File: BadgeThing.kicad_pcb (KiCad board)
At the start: 2 copper layers, 78.7 x 40.2 mm, 67 parts, among them J1 USB_C_Receptacle_USB2.0, J2 Connector_Generic_Conn_01x02, J3 Ext 5V, J4 SWD Header, J6 External 3V3, SW1 BOOTSEL, SW2 ESP RESET, SW3 Left, SW4 Down, SW5 Select, SW6 Up, SW7 Right, U2 W25Q32JVSS, U3 RP2040, U4 NCP1117-3.3_SOT223, U5 ESP-12F, Y1 12.000MHz

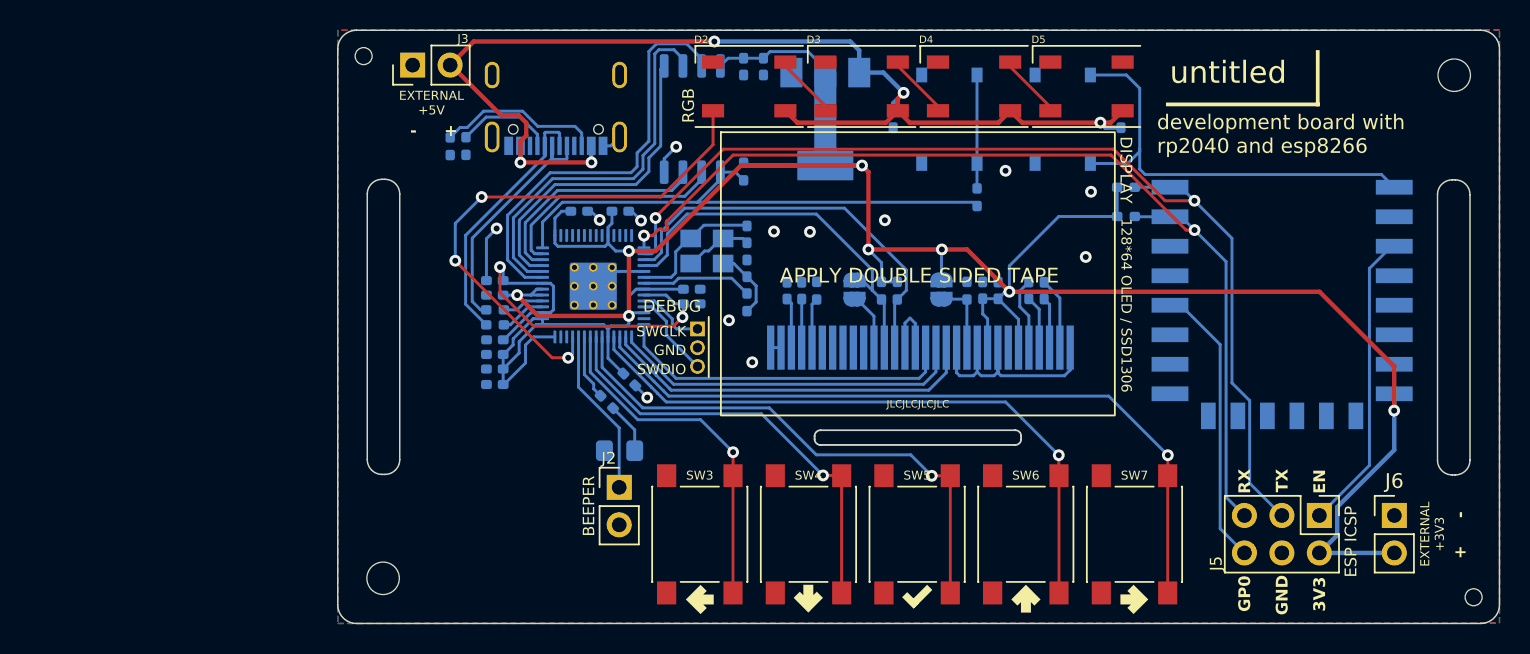
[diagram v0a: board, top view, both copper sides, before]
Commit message: Begin re-routing, updated ssd1306 pinout (not backwards anymore)
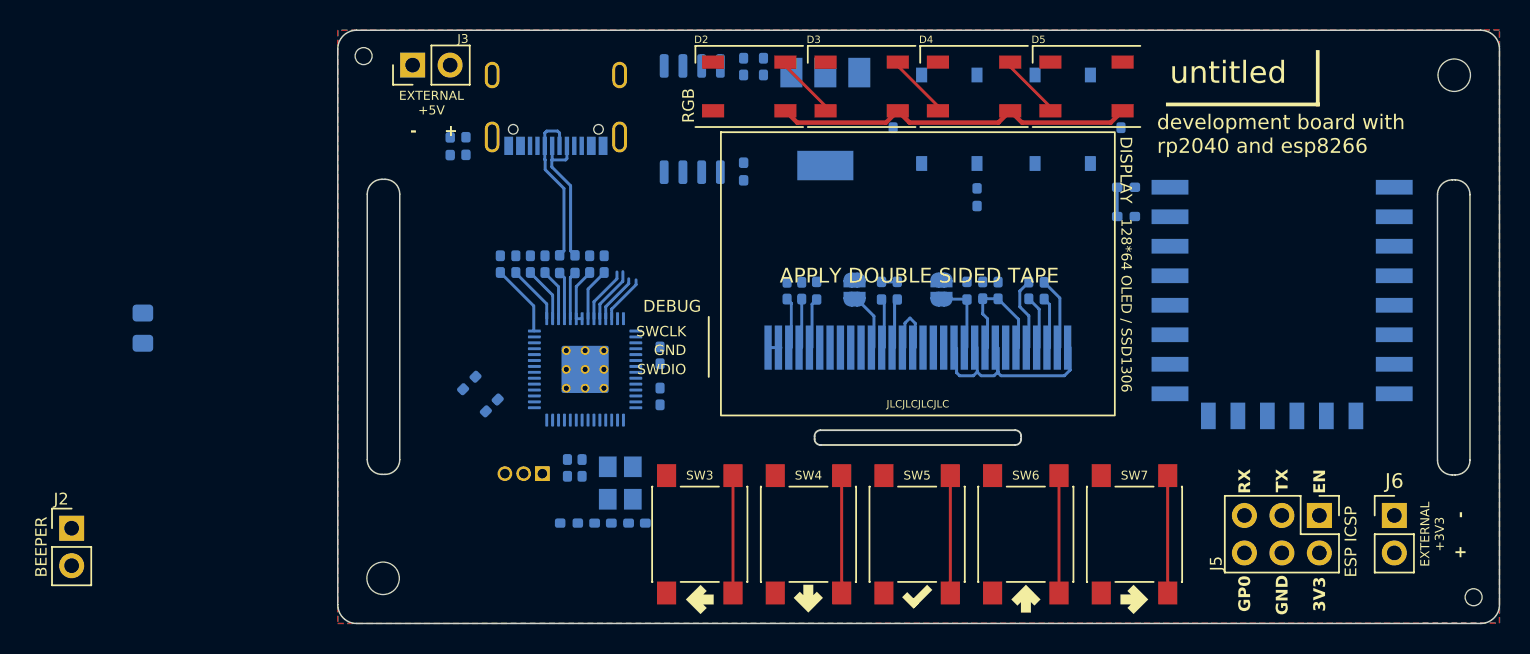
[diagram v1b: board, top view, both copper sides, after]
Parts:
- moved J2 37.2 mm to (104.4, 127.6)
- moved D1 33.4 mm to (109.2, 114.0), turned to -90 degrees
- moved C19 20.9 mm to (142.7, 127.3), turned to 0 degrees
- moved C20 19.8 mm to (140.4, 127.3), turned to 180 degrees
- moved R10 19.2 mm to (138.1, 127.3), turned to 0 degrees
- moved Y1 16.8 mm to (141.6, 124.5), turned to -90 degrees
- moved J4 14.4 mm to (136.3, 123.9), turned to 90 degrees
- moved C17 14.2 mm to (139.0, 123.5), turned to -90 degrees
- moved C8 14.0 mm to (138.0, 123.5), turned to -90 degrees
- moved C18 12.8 mm to (144.3, 118.7), turned to -90 degrees
- moved C22 11.2 mm to (144.3, 115.9), turned to -90 degrees
- moved C14 9.49 mm to (132.9, 119.3), turned to -135 degrees
- moved R7 9.41 mm to (131.3, 117.8), turned to -135 degrees
- moved C13 8.17 mm to (133.4, 109.7), turned to 90 degrees
- moved C7 7.50 mm to (140.5, 109.7), turned to 90 degrees
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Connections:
- U3 pad 15: ESP_RX -> MISO
- U3 pad 16: ESP_TX -> unconnected-(U3-GPIO13-Pad16)
- U3 pad 27: MISO -> unconnected-(U3-GPIO16-Pad27)
- U3 pad 6: unconnected-(U3-GPIO4-Pad6) -> ESP_RX
- U3 pad 7: unconnected-(U3-GPIO5-Pad7) -> ESP_TX
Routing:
- net +3V3: track 193.6 -> 28.0 mm, vias 8 -> 0
- net ESP_TX: track 71.2 -> 0.00 mm, vias 2 -> 0
- net ESP_RX: track 68.1 -> 0.00 mm, vias 2 -> 0
- net +5V: track 79.6 -> 24.8 mm, vias 5 -> 0
- net BTN5: track 50.2 -> 7.95 mm, vias 1 -> 0
- net WS2812B: track 36.4 -> 0.00 mm, vias 3 -> 0
- net QSPI_SS: track 36.3 -> 0.00 mm
- net BTN4: track 43.3 -> 7.95 mm, vias 1 -> 0
- net Net-(U5-~{RST}): track 30.8 -> 0.00 mm
- net BTN3: track 36.7 -> 7.95 mm, vias 1 -> 0
- net CS1: track 25.7 -> 0.00 mm
- net QSPI_SD3: track 28.9 -> 3.81 mm
- net RST: track 24.2 -> 0.00 mm
- net SCLK: track 27.4 -> 3.33 mm
- net DC: track 23.3 -> 0.00 mm
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
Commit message: Continue routing
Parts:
- added C24: 100nF, Capacitor_SMD:C_0402_1005Metric_Pad0.74x0.62mm_HandSolder, B.Cu at (138.8, 123.6)
- moved C10 9.87 mm to (143.1, 103.4)
- moved C14 9.71 mm to (134.5, 109.7), turned to 90 degrees
- moved C21 9.20 mm to (154.3, 105.0), turned to 180 degrees
- moved C15 8.72 mm to (131.9, 118.0), turned to 180 degrees
- moved J4 6.87 mm to (130.2, 127.2)
- moved R4 4.93 mm to (151.2, 108.2)
- moved C20 3.93 mm to (144.3, 127.8), turned to -90 degrees
- moved C19 3.14 mm to (140.7, 124.9), turned to 180 degrees
- moved C17 2.84 mm to (136.2, 123.6)
- moved C22 2.69 mm to (146.4, 114.2), turned to 0 degrees
- moved Y1 2.63 mm to (141.6, 127.2), turned to 0 degrees
- moved C18 2.29 mm to (146.4, 117.8), turned to 0 degrees
- moved R7 1.84 mm to (131.9, 116.0), turned to 180 degrees
- moved R10 0.92 mm to (138.9, 127.8), turned to 90 degrees
- moved C8 0.24 mm to (137.8, 123.6)
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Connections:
- U3 pad 15: MISO -> ESP_RX
- U3 pad 16: unconnected-(U3-GPIO13-Pad16) -> ESP_TX
- U3 pad 27: unconnected-(U3-GPIO16-Pad27) -> MISO
- U3 pad 6: ESP_RX -> unconnected-(U3-GPIO4-Pad6)
- U3 pad 7: ESP_TX -> unconnected-(U3-GPIO5-Pad7)
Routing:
- net +5V: track 24.8 -> 67.8 mm, vias 0 -> 1
- net +3V3: track 28.0 -> 57.6 mm, vias 0 -> 2
- net QSPI_SS: track 0.00 -> 28.2 mm
- net QSPI_SD1: track 0.00 -> 26.1 mm
- net QSPI_SD2: track 3.32 -> 24.0 mm
- net QSPI_SD0: track 3.35 -> 13.2 mm
- net +1V1: track 7.09 -> 16.1 mm, vias 0 -> 2
- net QSPI_SCLK: track 3.84 -> 12.8 mm
- net QSPI_SD3: track 3.81 -> 12.5 mm
- net XOUT: track 0.00 -> 7.12 mm
- net XIN: track 0.00 -> 6.33 mm
- net Net-(C20-Pad2): track 0.00 -> 6.26 mm
- net GND: track 21.6 -> 25.4 mm
- net SWCLK: track 0.00 -> 3.81 mm
- net SWDIO: track 0.00 -> 3.67 mm
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- added copper zone on B.Cu, net +1V1
- added copper zone on B.Cu, net +3V3

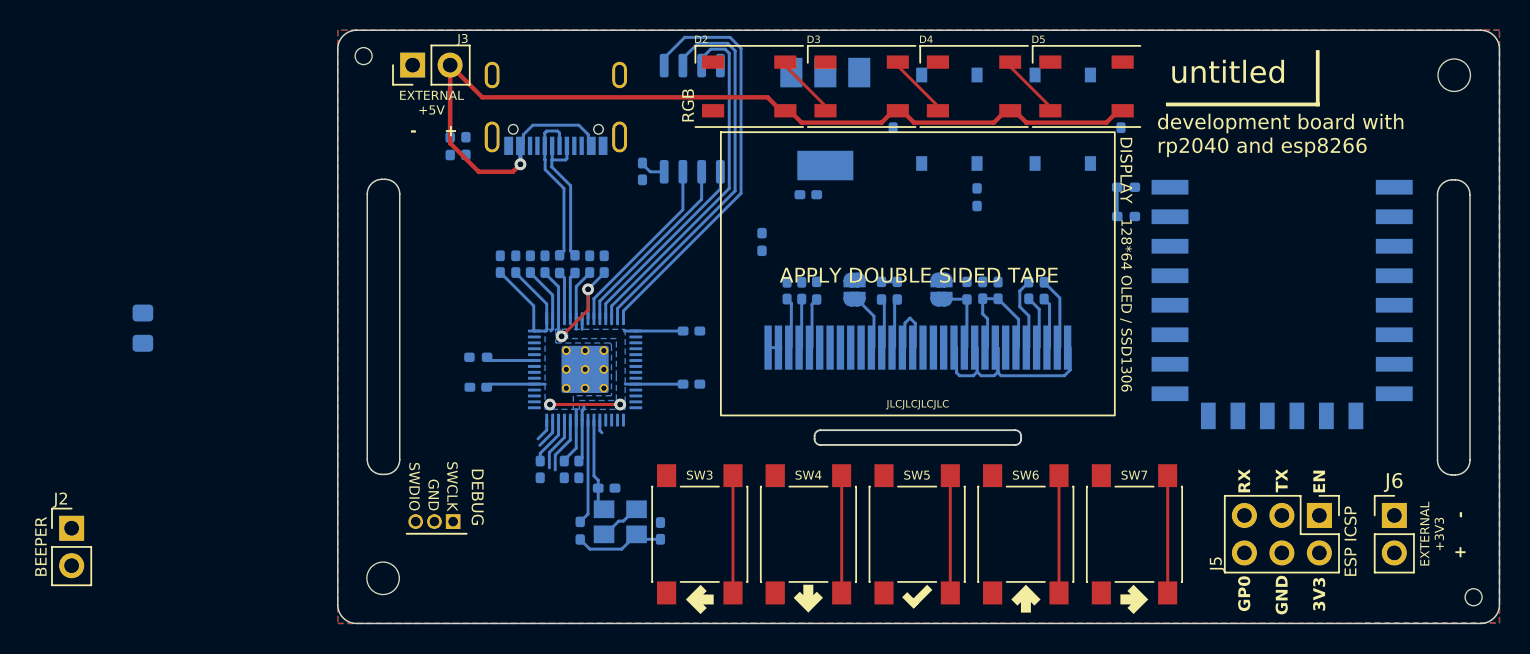
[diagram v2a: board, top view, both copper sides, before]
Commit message: huge routing optimizations and extra features
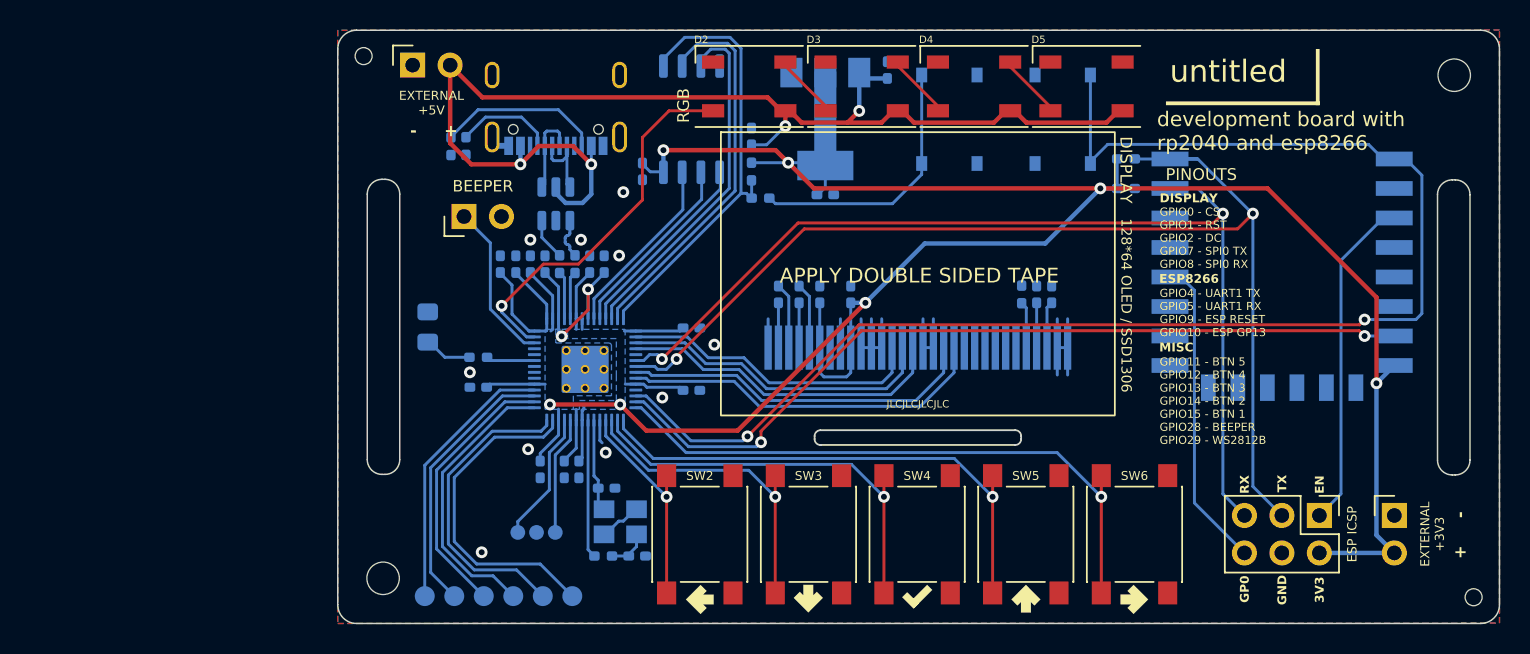
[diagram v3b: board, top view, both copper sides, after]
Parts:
- removed JP1, JP2: SolderJumper_2_Open, Jumper:SolderJumper-2_P1.3mm_Open_RoundedPad1.0x1.5mm
- removed the R1 at (165.1, 111.5)
- removed the R11 at (160.4, 111.5)
- removed R12: DNF, Resistor_SMD:R_0402_1005Metric_Pad0.72x0.64mm_HandSolder
- added J7: Conn_01x06, Connector_PinHeader_2.00mm:PinHeader_1x06_P2.00mm_Vertical, B.Cu at (138.3, 132.2)
- added U6: USBLC6-2SC6, Package_TO_SOT_SMD:SOT-23-6, B.Cu at (137.2, 105.6)
- moved J6 34.0 mm to (131.0, 106.5), turned to 90 degrees
- moved C16 25.1 mm to (150.5, 101.0)
- moved D1 19.3 mm to (128.5, 114.0)
- moved C3 18.0 mm to (152.3, 111.8), turned to -90 degrees
- moved C2 17.9 mm to (170.8, 111.8)
- moved C6 15.9 mm to (169.8, 111.8)
- moved C1 15.6 mm to (153.7, 111.8)
- moved R8 14.7 mm to (151.1, 105.2), turned to 180 degrees
- moved R1 13.9 mm to (168.8, 111.8)
- moved C4 11.0 mm to (155.1, 111.8)
- moved C5 9.99 mm to (157.2, 111.8)
- moved J4 6.96 mm to (137.2, 127.9)
- moved R9 4.83 mm to (150.5, 103.4)
- moved C21 3.36 mm to (159.7, 96.6), turned to 90 degrees
- moved C19 2.32 mm to (142.7, 129.5), turned to 180 degrees
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- renumbered C2 to C1, C11 to C10, C12 to C11, C13 to C12, C14 to C13, C15 to C14, C17 to C15, C23 to C16, C18 to C17, C19 to C18, C20 to C19, C6 to C2, C22 to C20, C16 to C21, C24 to C22, C21 to C23, C10 to C24, C1 to C3, C3 to C4, C4 to C5, C5 to C6, J5 to J1, J3 to J2, J6 to J3, J1 to J5, J2 to J6, R2 to R1, R8 to R10, R9 to R11, R13 to R2, R14 to R3, R5 to R4, R6 to R5, R7 to R6, R10 to R7, R3 to R8, R4 to R9, SW2 to SW1, SW3 to SW2, SW4 to SW3, SW5 to SW4, SW6 to SW5, SW7 to SW6, SW1 to SW7, U5 to U1, U1 to U2, U2 to U5
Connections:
- R4 pad 2: USB D+ -> USB_DP
- R5 pad 2: USB D- -> USB_DN
- SW1 pad 2: Net-(U5-~{RST}) -> ESP_RST
- U1 pad 1: Net-(U5-~{RST}) -> ESP_RST
- U1 pad 7: unconnected-(U5-GPIO13-Pad7) -> ESP13
- U2 pad 11: Net-(JP1-B) -> GND
- U2 pad 20: Net-(JP2-B) -> unconnected-(U2-D2/I2C_SDA-Pad20)
- U3 pad 11: unconnected-(U3-GPIO8-Pad11) -> MISO
- U3 pad 12: unconnected-(U3-GPIO9-Pad12) -> ESP_RST
- U3 pad 13: unconnected-(U3-GPIO10-Pad13) -> ESP13
- U3 pad 14: unconnected-(U3-GPIO11-Pad14) -> BTN5
- U3 pad 15: ESP_RX -> BTN4
- U3 pad 16: ESP_TX -> BTN3
- U3 pad 17: SCLK -> BTN2
- U3 pad 18: MOSI -> BTN1
- U3 pad 2: unconnected-(U3-GPIO0-Pad2) -> CS1
- U3 pad 27: MISO -> GP16
- U3 pad 28: DC -> GP17
- U3 pad 29: RST -> GP18
- U3 pad 3: unconnected-(U3-GPIO1-Pad3) -> RST
- U3 pad 30: CS1 -> GP19
- U3 pad 31: BTN5 -> GP20
- U3 pad 32: BTN4 -> GP21
- U3 pad 34: BTN3 -> unconnected-(U3-GPIO22-Pad34)
- U3 pad 35: BTN2 -> unconnected-(U3-GPIO23-Pad35)
- U3 pad 36: BTN1 -> unconnected-(U3-GPIO24-Pad36)
- U3 pad 38: BEEP -> unconnected-(U3-GPIO26_ADC0-Pad38)
- U3 pad 39: WS2812B -> unconnected-(U3-GPIO27_ADC1-Pad39)
- U3 pad 4: unconnected-(U3-GPIO2-Pad4) -> DC
- U3 pad 40: unconnected-(U3-GPIO28_ADC2-Pad40) -> BEEP
- U3 pad 41: unconnected-(U3-GPIO29_ADC3-Pad41) -> WS2812B
- U3 pad 6: unconnected-(U3-GPIO4-Pad6) -> ESP_RX
- U3 pad 7: unconnected-(U3-GPIO5-Pad7) -> ESP_TX
- U3 pad 8: unconnected-(U3-GPIO6-Pad8) -> SCLK
- U3 pad 9: unconnected-(U3-GPIO7-Pad9) -> MOSI
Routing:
- net +3V3: track 57.6 -> 195.6 mm, vias 2 -> 7
- net ESP_RST: track 0.00 -> 97.4 mm, vias 0 -> 2
- net ESP_TX: track 0.00 -> 79.0 mm, vias 0 -> 2
- net ESP_RX: track 0.00 -> 71.9 mm, vias 0 -> 2
- net ESP13: track 0.00 -> 56.5 mm, vias 0 -> 2
- net BTN5: track 7.95 -> 42.0 mm, vias 0 -> 1
- net BTN4: track 7.95 -> 35.5 mm, vias 0 -> 1
- net WS2812B: track 0.00 -> 25.6 mm, vias 0 -> 1
- net ESP_EN: track 0.00 -> 22.7 mm
- net GP16: track 0.00 -> 22.5 mm
- net MOSI: track 3.34 -> 25.0 mm
- net RST: track 0.00 -> 21.5 mm
- net ESP0: track 0.00 -> 21.2 mm
- net GP17: track 0.00 -> 21.0 mm
- net DC: track 1.52 -> 22.4 mm
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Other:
- board text added: "16"
- board text added: "17"
- board text added: "18"
- board text added: "19"
- board text added: "20"
- board text added: "21"
- board text added: "CLK"
- board text added: "GPIO0 - CS GPIO1 - RST GPIO2 - DC GPIO7 - SPI0 TX GPIO8 - SPI0 RX"
- board text added: "GPIO11 - BTN 5 GPIO12 - BTN 4 GPIO13 - BTN 3 GPIO14 - BTN 2 GPIO15 - BTN 1 GPIO28 - BEEPER GPIO29 - WS2812B"
- board text added: "GPIO4 - UART1 TX GPIO5 - UART1 RX GPIO9 - ESP RESET GPIO10 - ESP GP13"
- board text added: "IO"
- board text added: "MISC"
- board text added: "PINOUTS"
- board text removed: "BRIDGE JUMPERS TO CHANGE DISPLAY TO I2C MODE! WIRES WILL HAVE TO BE BODGED. TRY AT YOUR OWN RISK."
- board text removed: "DEBUG"
- board text removed: "SWCLK"
- board text removed: "SWDIO"
- board text removed: "mounting holes - m2 wristband slots - 20mm"

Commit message: Final routing
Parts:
- added R12: 4.7k, Resistor_SMD:R_0402_1005Metric_Pad0.72x0.64mm_HandSolder, B.Cu at (160.7, 111.8)
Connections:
- U3 pad 34: unconnected-(U3-GPIO22-Pad34) -> ESP0
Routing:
- net ESP0: track 21.2 -> 93.7 mm, vias 0 -> 2
- net RST: track 21.5 -> 24.5 mm
- net ESP_RX: track 71.9 -> 74.3 mm
- net +3V3: track 195.6 -> 196.5 mm
- net GND: vias 10 -> 8
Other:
- board text added: "GP16"
- board text added: "GP17"
- board text added: "GP18"
- board text added: "GP19"
- board text added: "GP20"
- board text added: "GP21"
- board text added: "GPIO"
- board text added: "SWDIO"
- board text removed: "16"
- board text removed: "17"
- board text removed: "18"
- board text removed: "19"
- board text removed: "20"
- board text removed: "21"
